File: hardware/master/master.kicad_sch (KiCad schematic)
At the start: 0 parts

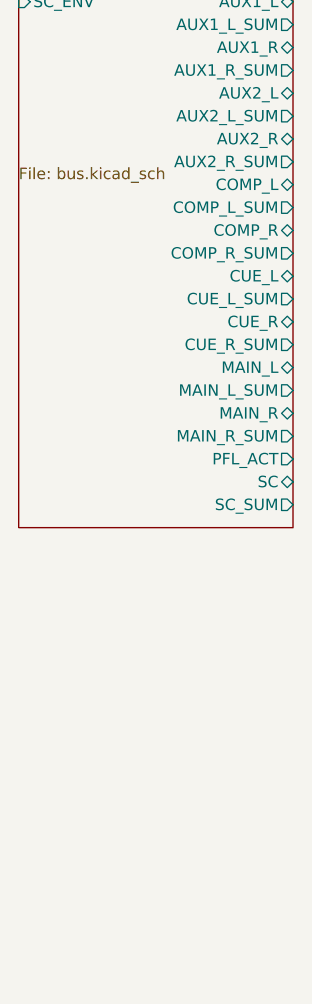
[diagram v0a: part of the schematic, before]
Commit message: Add master card power sheet
Power ribbon in from the power board, LM317/LM337 to +/-15.1 V, L7805
for the master's heavier +5 V LED load, the system AGND-PGND star point
as a net tie, and the frame bond with ground lift (decision 87). Parts
whose project number starts with "none" stay out of the BOM.

Co-Authored-By: Claude Opus 5.5 <noreply@anthropic.com>
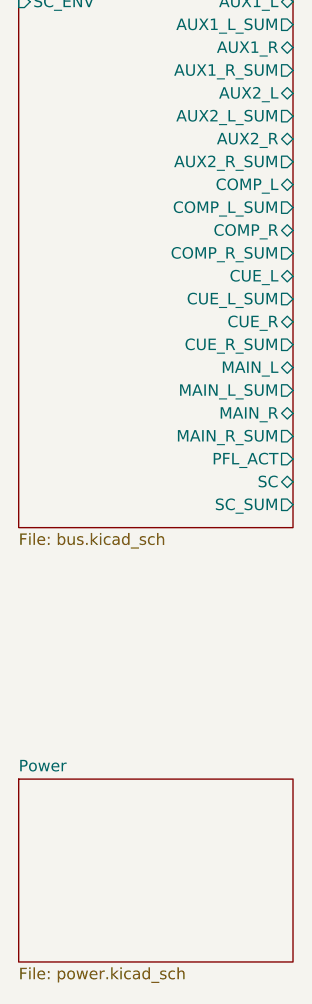
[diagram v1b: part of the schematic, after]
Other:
- added sheet Power (power.kicad_sch)
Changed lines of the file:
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@@
 		)
 		(property "Sheetfile" "bus.kicad_sch"
-			(at 25.4 59.0046 0)
+			(at 25.4 99.6446 0)
 			(effects
 				(font
@@
 		)
 		(pin "AUX1_L" bidirectional
-			(at 55.88 40.64 0)
+			(at 55.88 40.64 0.0000)
 			(effects
 				(font
@@
 		)
 		(pin "AUX1_L_SUM" output
-			(at 55.88 43.18 0)
+			(at 55.88 43.18 0.0000)
 			(effects
 				(font
@@
 		)
 		(pin "AUX1_R" bidirectional
-			(at 55.88 45.72 0)
+			(at 55.88 45.72 0.0000)
 			(effects
 				(font
@@
 		)
 		(pin "AUX1_R_SUM" output
-			(at 55.88 48.26 0)
+			(at 55.88 48.26 0.0000)
 			(effects
 				(font
@@
 		)
 		(pin "AUX2_L" bidirectional
-			(at 55.88 50.8 0)
+			(at 55.88 50.8 0.0000)
 			(effects
 				(font
@@
 		)
 		(pin "AUX2_L_SUM" output
-			(at 55.88 53.34 0)
+			(at 55.88 53.34 0.0000)
 			(effects
 				(font
@@
 		)
 		(pin "AUX2_R" bidirectional
-			(at 55.88 55.88 0)
+			(at 55.88 55.88 0.0000)
 			(effects
 				(font
@@
 		)
 		(pin "AUX2_R_SUM" output
-			(at 55.88 58.42 0)
+			(at 55.88 58.42 0.0000)
 			(effects
 				(font
@@
 		)
 		(pin "COMP_L" bidirectional
-			(at 55.88 60.96 0)
+			(at 55.88 60.96 0.0000)
 			(effects
 				(font
@@
 		)
 		(pin "COMP_L_SUM" output
-			(at 55.88 63.5 0)
+			(at 55.88 63.5 0.0000)
 			(effects
 				(font
@@
 		)
 		(pin "COMP_R" bidirectional
-			(at 55.88 66.04 0)
+			(at 55.88 66.04 0.0000)
 			(effects
 				(font
@@
 		)
 		(pin "COMP_R_SUM" output
-			(at 55.88 68.58 0)
+			(at 55.88 68.58 0.0000)
 			(effects
 				(font
@@
 		)
 		(pin "CUE_L" bidirectional
-			(at 55.88 71.12 0)
+			(at 55.88 71.12 0.0000)
 			(effects
 				(font
@@
 		)
 		(pin "CUE_L_SUM" output
-			(at 55.88 73.66 0)
+			(at 55.88 73.66 0.0000)
 			(effects
 				(font
@@
 		)
 		(pin "CUE_R" bidirectional
-			(at 55.88 76.2 0)
+			(at 55.88 76.2 0.0000)
 			(effects
 				(font
@@
 		)
 		(pin "CUE_R_SUM" output
-			(at 55.88 78.74 0)
+			(at 55.88 78.74 0.0000)
 			(effects
 				(font
@@
 		)
 		(pin "MAIN_L" bidirectional
-			(at 55.88 81.28 0)
+			(at 55.88 81.28 0.0000)
 			(effects
 				(font
@@
 		)
 		(pin "MAIN_L_SUM" output
-			(at 55.88 83.82 0)
+			(at 55.88 83.82 0.0000)
 			(effects
 				(font
@@
 		)
 		(pin "MAIN_R" bidirectional
-			(at 55.88 86.36 0)
+			(at 55.88 86.36 0.0000)
 			(effects
 				(font
@@
 		)
 		(pin "MAIN_R_SUM" output
-			(at 55.88 88.9 0)
+			(at 55.88 88.9 0.0000)
 			(effects
 				(font
@@
 		)
 		(pin "PFL_ACT" output
-			(at 55.88 91.44 0)
+			(at 55.88 91.44 0.0000)
 			(effects
 				(font
@@
 		)
 		(pin "SC" bidirectional
-			(at 55.88 93.98 0)
+			(at 55.88 93.98 0.0000)
 			(effects
 				(font
@@
 		)
 		(pin "SC_SUM" output
-			(at 55.88 96.52 0)
+			(at 55.88 96.52 0.0000)
 			(effects
 				(font
@@
 				)
 			)
+		)
+	)
+	(sheet
+		(at 25.4 127)
+		(size 30.48 20.32)
+		(exclude_from_sim no)
+		(in_bom yes)
+		(on_board yes)
+		(dnp no)
+		(fields_autoplaced yes)
+		(stroke
+			(width 0.1524)
+			(type solid)
+		)
+		(fill
+			(color 0 0 0 0.0000)
+		)
+		(property "Sheetname" "Power"
+			(at 25.4 126.2884 0)
+			(effects
+				(font
+					(size 1.27 1.27)
+				)
+				(justify left bottom)
+			)
+		)
+		(property "Sheetfile" "power.kicad_sch"
+			(at 25.4 147.9046 0)
+			(effects
+				(font
+					(size 1.27 1.27)
+				)
+				(justify left top)
+			)
+		)
+		(instances
+			(project "master"
+				(path "/e58f7b8d-79d3-4449-9042-9214947ce872"
+					(page "3")
+				)
+			)

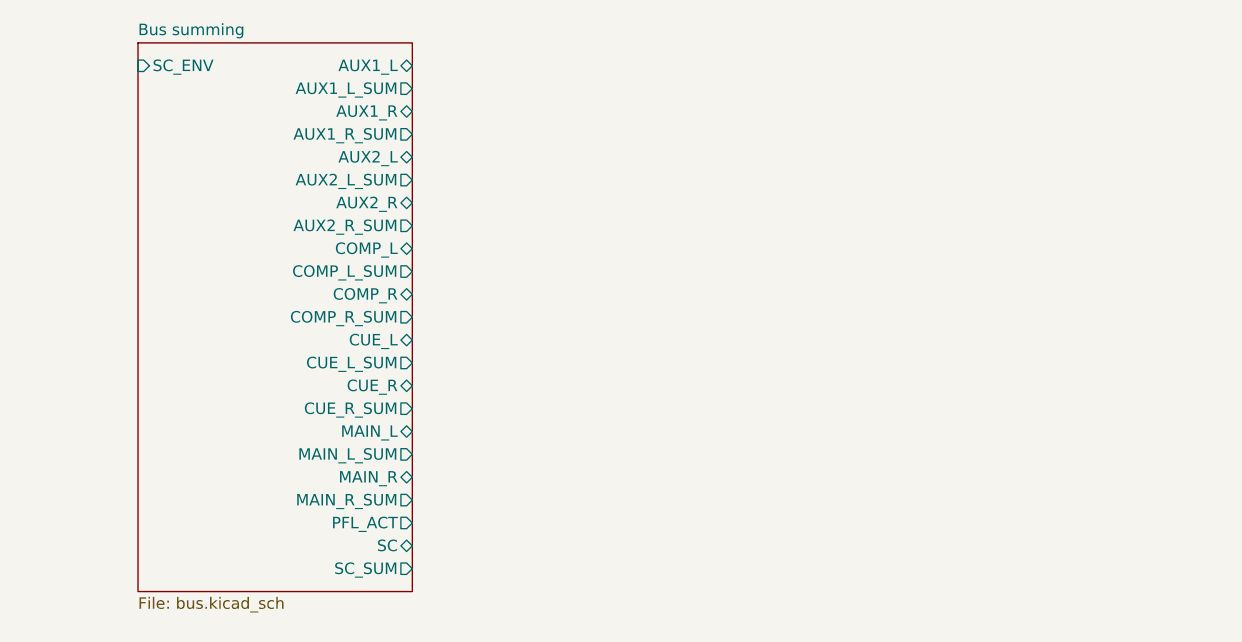
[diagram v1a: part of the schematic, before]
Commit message: Add master card AUX return sheets
Two identical return sheets from one script: L/MONO-normalled jacks,
AD8273 receiver with a PRO/PEDAL gain jumper after it, SSI2162 VCA with
the channel fader law on a level pot, DG413 mute and duck, inverter and
22k bus resistors switched to MAIN or COMP (decision 88). Checked
against aux_return_build.py; the master rebuild script now runs every
sheet script.

Co-Authored-By: Claude Opus 5.5 <noreply@anthropic.com>
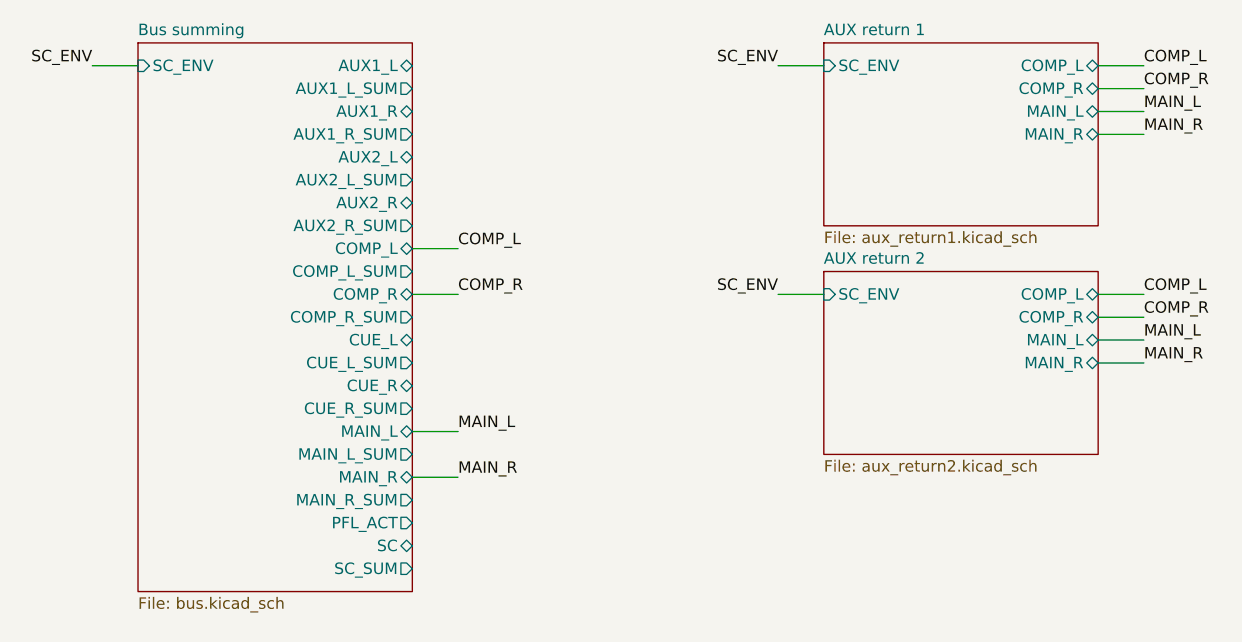
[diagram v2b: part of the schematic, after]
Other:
- added sheet AUX return 1 (aux_return1.kicad_sch)
- added sheet AUX return 2 (aux_return2.kicad_sch)
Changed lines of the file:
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@@
 		)
 	)
+	(sheet
+		(at 101.6 38.1)
+		(size 30.48 20.32)
+		(exclude_from_sim no)
+		(in_bom yes)
+		(on_board yes)
+		(dnp no)
+		(fields_autoplaced yes)
+		(stroke
+			(width 0.1524)
+			(type solid)
+		)
+		(fill
+			(color 0 0 0 0.0000)
+		)
+		(property "Sheetname" "AUX return 1"
+			(at 101.6 37.3884 0)
+			(effects
+				(font
+					(size 1.27 1.27)
+				)
+				(justify left bottom)
+			)
+		)
+		(property "Sheetfile" "aux_return1.kicad_sch"
+			(at 101.6 59.0046 0)
+			(effects
+				(font
+					(size 1.27 1.27)
+				)
+				(justify left top)
+			)
+		)
+		(pin "SC_ENV" input
+			(at 101.6 40.64 180)
+			(effects
+				(font
+					(size 1.27 1.27)
+				)
+				(justify left)
+			)
+		)
+		(pin "COMP_L" bidirectional
+			(at 132.08 40.64 0.0000)
+			(effects
+				(font
+					(size 1.27 1.27)
+				)
+				(justify right)
+			)
+		)
+		(pin "COMP_R" bidirectional
+			(at 132.08 43.18 0.0000)
+			(effects
+				(font
+					(size 1.27 1.27)
+				)
+				(justify right)
+			)
+		)
+		(pin "MAIN_L" bidirectional
+			(at 132.08 45.72 0.0000)
+			(effects
+				(font
+					(size 1.27 1.27)
+				)
+				(justify right)
+			)
+		)
+		(pin "MAIN_R" bidirectional
+			(at 132.08 48.26 0.0000)
+			(effects
+				(font
+					(size 1.27 1.27)
+				)
+				(justify right)
+			)
+		)
+		(instances
+			(project "master"
+				(path "/e58f7b8d-79d3-4449-9042-9214947ce872"
+					(page "4")
+				)
+			)
+		)
+	)
+	(sheet
+		(at 101.6 63.5)
+		(size 30.48 20.32)
+		(exclude_from_sim no)
+		(in_bom yes)
+		(on_board yes)
+		(dnp no)
+		(fields_autoplaced yes)
+		(stroke
+			(width 0.1524)
+			(type solid)
+		)
+		(fill
+			(color 0 0 0 0.0000)
+		)
+		(property "Sheetname" "AUX return 2"
+			(at 101.6 62.7884 0)
+			(effects
+				(font
+					(size 1.27 1.27)
+				)
+				(justify left bottom)
+			)
+		)
+		(property "Sheetfile" "aux_return2.kicad_sch"
+			(at 101.6 84.4046 0)
+			(effects
+				(font
+					(size 1.27 1.27)
+				)
+				(justify left top)
+			)
+		)
+		(pin "SC_ENV" input
+			(at 101.6 66.04 180)
+			(effects
+				(font
+					(size 1.27 1.27)
+				)
+				(justify left)
+			)
+		)
+		(pin "COMP_L" bidirectional
+			(at 132.08 66.04 0)
+			(effects
+				(font
+					(size 1.27 1.27)
+				)
+				(justify right)
+			)
+		)
+		(pin "COMP_R" bidirectional
+			(at 132.08 68.58 0)
+			(effects
+				(font
+					(size 1.27 1.27)
+				)
+				(justify right)
+			)
+		)
+		(pin "MAIN_L" bidirectional
+			(at 132.08 71.12 0)
+			(effects
+				(font
+					(size 1.27 1.27)
+				)
+				(justify right)
+			)
+		)
+		(pin "MAIN_R" bidirectional
+			(at 132.08 73.66 0)
+			(effects
+				(font
+					(size 1.27 1.27)
+				)
+				(justify right)
+			)
+		)
+		(instances
+			(project "master"
+				(path "/e58f7b8d-79d3-4449-9042-9214947ce872"
+					(page "5")
+				)
+			)
+		)
+	)
+	(wire (pts (xy 25.4 40.64) (xy 20.32 40.64)) (stroke (width 0) (type default)))
+	(label "SC_ENV" (at 20.32 40.64 180) (fields_autoplaced yes) (effects (font (size 1.27 1.27)) (justify right bottom)))
+	(wire (pts (xy 55.88 60.96) (xy 60.96 60.96)) (stroke (width 0) (type default)))
+	(label "COMP_L" (at 60.96 60.96 0) (fields_autoplaced yes) (effects (font (size 1.27 1.27)) (justify left bottom)))
+	(wire (pts (xy 55.88 66.04) (xy 60.96 66.04)) (stroke (width 0) (type default)))
+	(label "COMP_R" (at 60.96 66.04 0) (fields_autoplaced yes) (effects (font (size 1.27 1.27)) (justify left bottom)))
+	(wire (pts (xy 55.88 81.28) (xy 60.96 81.28)) (stroke (width 0) (type default)))
+	(label "MAIN_L" (at 60.96 81.28 0) (fields_autoplaced yes) (effects (font (size 1.27 1.27)) (justify left bottom)))
+	(wire (pts (xy 55.88 86.36) (xy 60.96 86.36)) (stroke (width 0) (type default)))
+	(label "MAIN_R" (at 60.96 86.36 0) (fields_autoplaced yes) (effects (font (size 1.27 1.27)) (justify left bottom)))
+	(wire (pts (xy 101.6 40.64) (xy 96.52 40.64)) (stroke (width 0) (type default)))
+	(label "SC_ENV" (at 96.52 40.64 180) (fields_autoplaced yes) (effects (font (size 1.27 1.27)) (justify right bottom)))
+	(wire (pts (xy 132.08 40.64) (xy 137.16 40.64)) (stroke (width 0) (type default)))
+	(label "COMP_L" (at 137.16 40.64 0) (fields_autoplaced yes) (effects (font (size 1.27 1.27)) (justify left bottom)))
+	(wire (pts (xy 132.08 43.18) (xy 137.16 43.18)) (stroke (width 0) (type default)))
+	(label "COMP_R" (at 137.16 43.18 0) (fields_autoplaced yes) (effects (font (size 1.27 1.27)) (justify left bottom)))
+	(wire (pts (xy 132.08 45.72) (xy 137.16 45.72)) (stroke (width 0) (type default)))
+	(label "MAIN_L" (at 137.16 45.72 0) (fields_autoplaced yes) (effects (font (size 1.27 1.27)) (justify left bottom)))
+	(wire (pts (xy 132.08 48.26) (xy 137.16 48.26)) (stroke (width 0) (type default)))
+	(label "MAIN_R" (at 137.16 48.26 0) (fields_autoplaced yes) (effects (font (size 1.27 1.27)) (justify left bottom)))
+	(wire (pts (xy 101.6 66.04) (xy 96.52 66.04)) (stroke (width 0) (type default)))
+	(label "SC_ENV" (at 96.52 66.04 180) (fields_autoplaced yes) (effects (font (size 1.27 1.27)) (justify right bottom)))
+	(wire (pts (xy 132.08 66.04) (xy 137.16 66.04)) (stroke (width 0) (type default)))
+	(label "COMP_L" (at 137.16 66.04 0) (fields_autoplaced yes) (effects (font (size 1.27 1.27)) (justify left bottom)))
+	(wire (pts (xy 132.08 68.58) (xy 137.16 68.58)) (stroke (width 0) (type default)))
+	(label "COMP_R" (at 137.16 68.58 0) (fields_autoplaced yes) (effects (font (size 1.27 1.27)) (justify left bottom)))
+	(wire (pts (xy 132.08 71.12) (xy 137.16 71.12)) (stroke (width 0) (type default)))
+	(label "MAIN_L" (at 137.16 71.12 0) (fields_autoplaced yes) (effects (font (size 1.27 1.27)) (justify left bottom)))
+	(wire (pts (xy 132.08 73.66) (xy 137.16 73.66)) (stroke (width 0) (type default)))
+	(label "MAIN_R" (at 137.16 73.66 0) (fields_autoplaced yes) (effects (font (size 1.27 1.27)) (justify left bottom)))
 	(sheet_instances
 		(path "/"

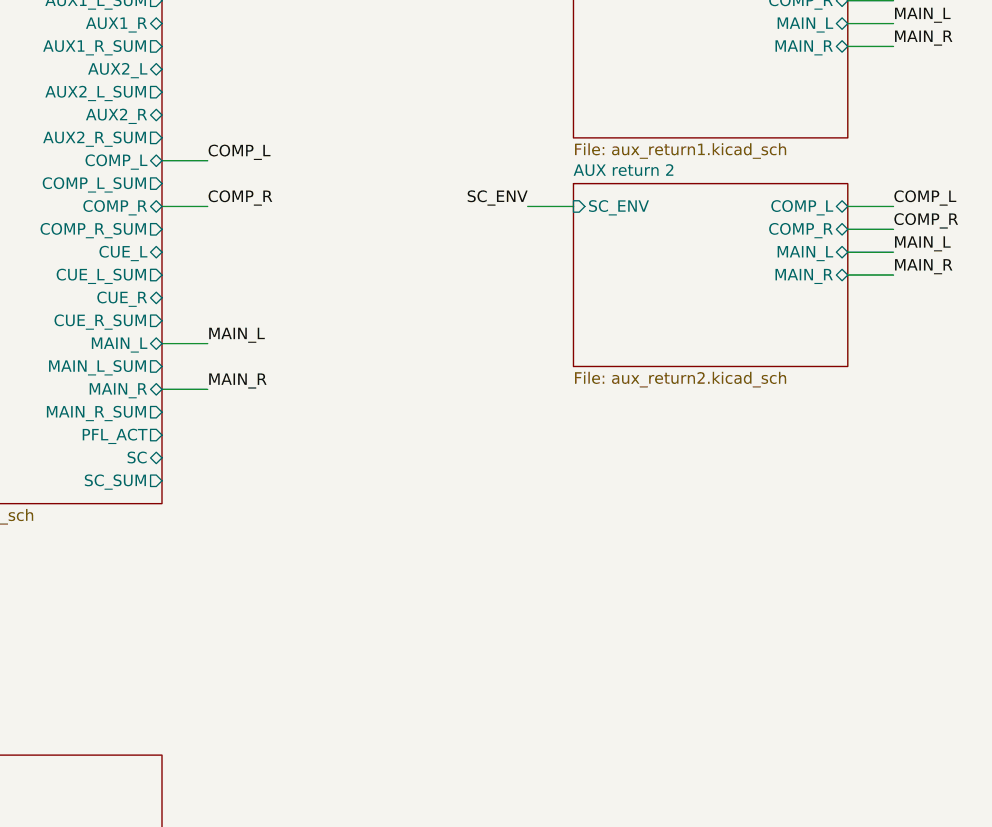
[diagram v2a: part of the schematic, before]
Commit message: Add master card compressor sheet
Log-domain peak detector on the AS3046D matched pair with ERA-V33
temperature compensation, current-mirror release, 4:1 gain computer
with Amount-linked makeup, click-free on/off ramp, MIX crossfade and
gain-reduction LEDs (decision 89). Side chain simulated in ngspice
(simulation/compressor). Adds the AS3046 symbol, verified DG413 unit
mapping and a session handoff file.

Co-Authored-By: Claude Opus 5.5 <noreply@anthropic.com>
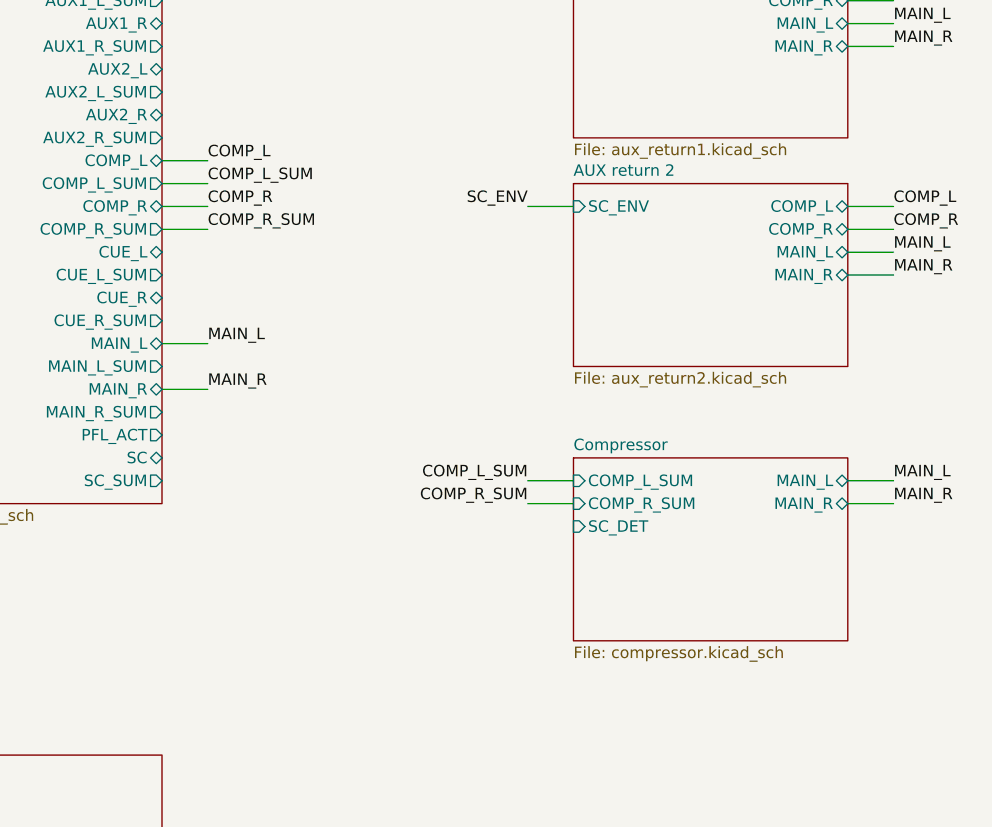
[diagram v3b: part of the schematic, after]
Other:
- added sheet Compressor (compressor.kicad_sch)
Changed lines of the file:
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@@
 		)
 		(pin "COMP_L" bidirectional
-			(at 132.08 66.04 0)
+			(at 132.08 66.04 0.0000)
 			(effects
 				(font
@@
 		)
 		(pin "COMP_R" bidirectional
-			(at 132.08 68.58 0)
+			(at 132.08 68.58 0.0000)
 			(effects
 				(font
@@
 		)
 		(pin "MAIN_L" bidirectional
-			(at 132.08 71.12 0)
+			(at 132.08 71.12 0.0000)
 			(effects
 				(font
@@
 		)
 		(pin "MAIN_R" bidirectional
-			(at 132.08 73.66 0)
+			(at 132.08 73.66 0.0000)
 			(effects
 				(font
@@
 		)
 	)
+	(sheet
+		(at 101.6 93.98)
+		(size 30.48 20.32)
+		(exclude_from_sim no)
+		(in_bom yes)
+		(on_board yes)
+		(dnp no)
+		(fields_autoplaced yes)
+		(stroke
+			(width 0.1524)
+			(type solid)
+		)
+		(fill
+			(color 0 0 0 0.0000)
+		)
+		(property "Sheetname" "Compressor"
+			(at 101.6 93.2684 0)
+			(effects
+				(font
+					(size 1.27 1.27)
+				)
+				(justify left bottom)
+			)
+		)
+		(property "Sheetfile" "compressor.kicad_sch"
+			(at 101.6 114.8846 0)
+			(effects
+				(font
+					(size 1.27 1.27)
+				)
+				(justify left top)
+			)
+		)
+		(pin "COMP_L_SUM" input
+			(at 101.6 96.52 180)
+			(effects
+				(font
+					(size 1.27 1.27)
+				)
+				(justify left)
+			)
+		)
+		(pin "COMP_R_SUM" input
+			(at 101.6 99.06 180)
+			(effects
+				(font
+					(size 1.27 1.27)
+				)
+				(justify left)
+			)
+		)
+		(pin "SC_DET" input
+			(at 101.6 101.6 180)
+			(effects
+				(font
+					(size 1.27 1.27)
+				)
+				(justify left)
+			)
+		)
+		(pin "MAIN_L" bidirectional
+			(at 132.08 96.52 0)
+			(effects
+				(font
+					(size 1.27 1.27)
+				)
+				(justify right)
+			)
+		)
+		(pin "MAIN_R" bidirectional
+			(at 132.08 99.06 0)
+			(effects
+				(font
+					(size 1.27 1.27)
+				)
+				(justify right)
+			)
+		)
+		(instances
+			(project "master"
+				(path "/e58f7b8d-79d3-4449-9042-9214947ce872"
+					(page "6")
+				)
+			)
+		)
+	)
 	(wire (pts (xy 25.4 40.64) (xy 20.32 40.64)) (stroke (width 0) (type default)))
 	(label "SC_ENV" (at 20.32 40.64 180) (fields_autoplaced yes) (effects (font (size 1.27 1.27)) (justify right bottom)))
 	(wire (pts (xy 55.88 60.96) (xy 60.96 60.96)) (stroke (width 0) (type default)))
 	(label "COMP_L" (at 60.96 60.96 0) (fields_autoplaced yes) (effects (font (size 1.27 1.27)) (justify left bottom)))
+	(wire (pts (xy 55.88 63.5) (xy 60.96 63.5)) (stroke (width 0) (type default)))
+	(label "COMP_L_SUM" (at 60.96 63.5 0) (fields_autoplaced yes) (effects (font (size 1.27 1.27)) (justify left bottom)))
 	(wire (pts (xy 55.88 66.04) (xy 60.96 66.04)) (stroke (width 0) (type default)))
 	(label "COMP_R" (at 60.96 66.04 0) (fields_autoplaced yes) (effects (font (size 1.27 1.27)) (justify left bottom)))
+	(wire (pts (xy 55.88 68.58) (xy 60.96 68.58)) (stroke (width 0) (type default)))
+	(label "COMP_R_SUM" (at 60.96 68.58 0) (fields_autoplaced yes) (effects (font (size 1.27 1.27)) (justify left bottom)))
 	(wire (pts (xy 55.88 81.28) (xy 60.96 81.28)) (stroke (width 0) (type default)))
 	(label "MAIN_L" (at 60.96 81.28 0) (fields_autoplaced yes) (effects (font (size 1.27 1.27)) (justify left bottom)))
@@
 	(wire (pts (xy 132.08 73.66) (xy 137.16 73.66)) (stroke (width 0) (type default)))
 	(label "MAIN_R" (at 137.16 73.66 0) (fields_autoplaced yes) (effects (font (size 1.27 1.27)) (justify left bottom)))
+	(wire (pts (xy 101.6 96.52) (xy 96.52 96.52)) (stroke (width 0) (type default)))
+	(label "COMP_L_SUM" (at 96.52 96.52 180) (fields_autoplaced yes) (effects (font (size 1.27 1.27)) (justify right bottom)))
+	(wire (pts (xy 101.6 99.06) (xy 96.52 99.06)) (stroke (width 0) (type default)))
+	(label "COMP_R_SUM" (at 96.52 99.06 180) (fields_autoplaced yes) (effects (font (size 1.27 1.27)) (justify right bottom)))
+	(wire (pts (xy 132.08 96.52) (xy 137.16 96.52)) (stroke (width 0) (type default)))
+	(label "MAIN_L" (at 137.16 96.52 0) (fields_autoplaced yes) (effects (font (size 1.27 1.27)) (justify left bottom)))
+	(wire (pts (xy 132.08 99.06) (xy 137.16 99.06)) (stroke (width 0) (type default)))
+	(label "MAIN_R" (at 137.16 99.06 0) (fields_autoplaced yes) (effects (font (size 1.27 1.27)) (justify left bottom)))
 	(sheet_instances
 		(path "/"
